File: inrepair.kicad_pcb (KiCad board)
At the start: 2 copper layers, 81.3 x 31.8 mm, 4 parts, among them J1 EXTRAS, J2 POWER_FROM_ENID, U1 Pico

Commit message: Added URL to PCB; added images.
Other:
- board text added: "github.com/mackiea/ InformationalNabuRemoteEnidPicoActiveInterfaceRelay"

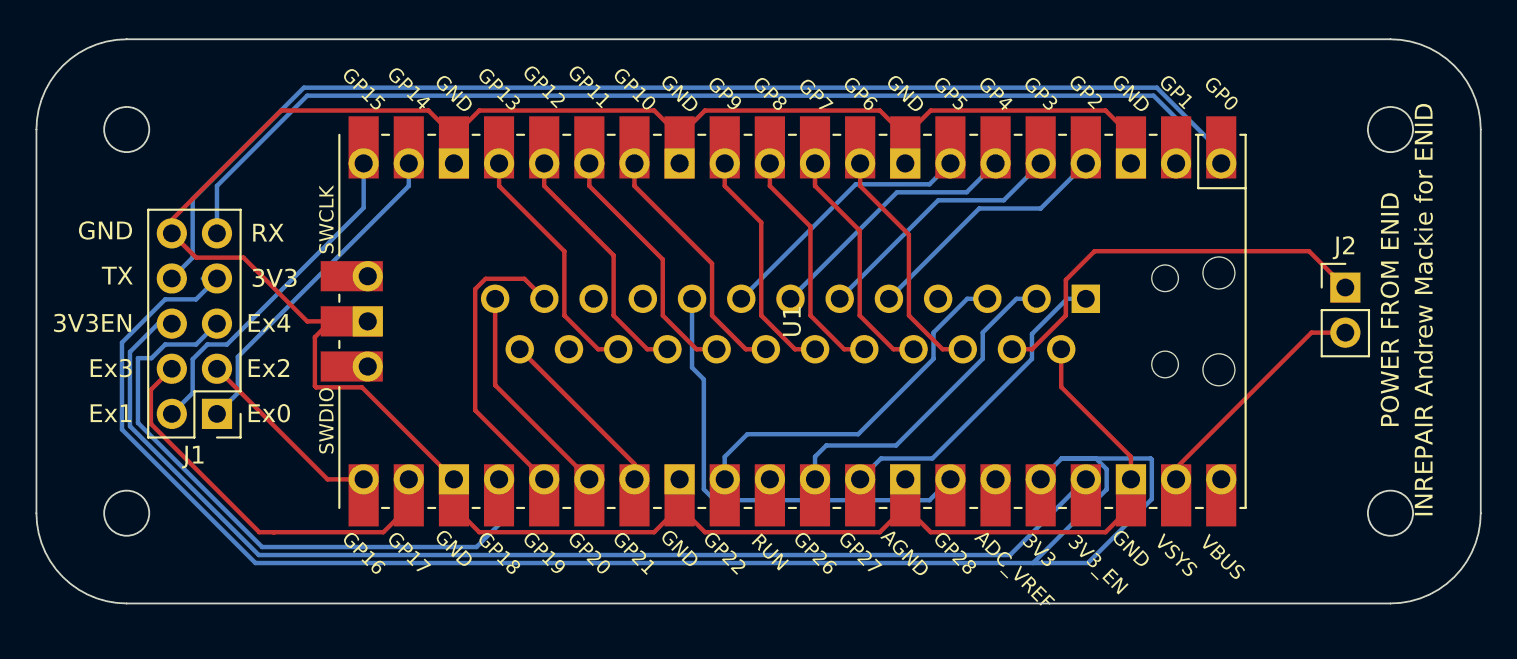
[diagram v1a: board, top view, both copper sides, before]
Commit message: ENID wconnector connections were reversed. Oopsie poopsie.
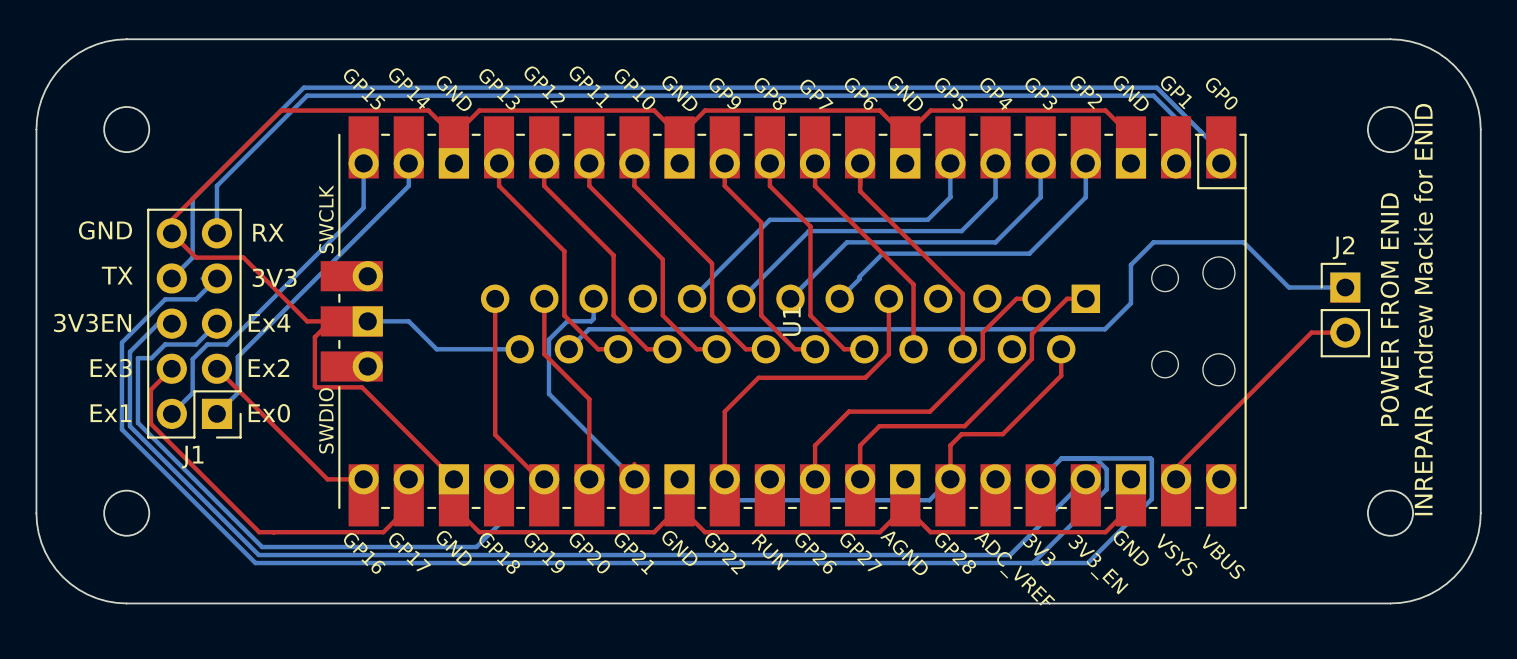
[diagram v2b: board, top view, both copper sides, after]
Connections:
- ENID1 pad 1: IO_REQUEST -> INTERRUPT_REQUEST
- ENID1 pad 10: AUDIO -> 1.79MhzClock
- ENID1 pad 11: 3.58MhzClock -> WRITE
- ENID1 pad 12: INTERRUPT_ACKNOWLEDGE -> READ
- ENID1 pad 13: INTERRUPT_REQUEST -> IO_REQUEST
- ENID1 pad 14: GND -> WAIT_REQUEST
- ENID1 pad 15: +5V_1 -> RESET
- ENID1 pad 16: DATA_7 -> DATA_0
- ENID1 pad 17: DATA_6 -> DATA_1
- ENID1 pad 18: DATA_5 -> DATA_2
- ENID1 pad 19: DATA_4 -> DATA_3
- ENID1 pad 2: READ -> INTERRUPT_ACKNOWLEDGE
- ENID1 pad 20: DATA_3 -> DATA_4
- ENID1 pad 21: DATA_2 -> DATA_5
- ENID1 pad 22: DATA_1 -> DATA_6
- ENID1 pad 23: DATA_0 -> DATA_7
- ENID1 pad 24: RESET -> +5V_1
- ENID1 pad 25: WAIT_REQUEST -> GND
- ENID1 pad 3: WRITE -> 3.58MhzClock
- ENID1 pad 4: 1.79MhzClock -> AUDIO
- ENID1 pad 5: ADDRESS_3 -> CARD_SELECT
- ENID1 pad 6: ADDRESS_2 -> ADDRESS_0
- ENID1 pad 8: ADDRESS_0 -> ADDRESS_2
- ENID1 pad 9: CARD_SELECT -> ADDRESS_3
- U1 pad 10: DATA_6 -> DATA_1
- U1 pad 11: DATA_5 -> DATA_2
- U1 pad 12: DATA_4 -> DATA_3
- U1 pad 14: DATA_3 -> DATA_4
- U1 pad 15: DATA_2 -> DATA_5
- U1 pad 16: DATA_1 -> DATA_6
- U1 pad 17: DATA_0 -> DATA_7
- U1 pad 25: INTERRUPT_ACKNOWLEDGE -> IO_REQUEST
- U1 pad 26: INTERRUPT_REQUEST -> READ
- U1 pad 27: WAIT_REQUEST -> WRITE
- U1 pad 29: WRITE -> CARD_SELECT
- U1 pad 31: READ -> INTERRUPT_ACKNOWLEDGE
- U1 pad 32: IO_REQUEST -> INTERRUPT_REQUEST
- U1 pad 34: CARD_SELECT -> WAIT_REQUEST
- U1 pad 4: ADDRESS_3 -> ADDRESS_0
- U1 pad 5: ADDRESS_2 -> ADDRESS_1
- U1 pad 6: ADDRESS_1 -> ADDRESS_2
- U1 pad 7: ADDRESS_0 -> ADDRESS_3
- U1 pad 9: DATA_7 -> DATA_0
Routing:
- net +5V_1: track 23.1 -> 48.5 mm
- net WAIT_REQUEST: track 9.99 -> 25.0 mm
- net CARD_SELECT: track 25.6 -> 17.5 mm
- net READ: track 18.3 -> 11.2 mm
- net INTERRUPT_REQUEST: track 12.4 -> 18.8 mm
- net IO_REQUEST: track 17.7 -> 11.5 mm
- net WRITE: track 20.6 -> 14.8 mm
- net ADDRESS_3: track 14.2 -> 18.9 mm
- net ADDRESS_2: track 14.5 -> 18.6 mm
- net ADDRESS_1: track 14.7 -> 18.4 mm
- net ADDRESS_0: track 14.9 -> 18.2 mm
- net INTERRUPT_ACKNOWLEDGE: track 16.9 -> 18.7 mm
- net DATA_1: track 14.0 -> 12.7 mm
- net DATA_4: track 13.2 -> 14.2 mm
- net DATA_3: track 14.2 -> 13.2 mm
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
